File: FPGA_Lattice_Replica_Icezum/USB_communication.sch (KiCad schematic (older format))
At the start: 38 parts, among them J1 USB_Micro_Type_B, U3 FT2232H, U4 DSC1001, U5 93LC56C

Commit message: se finalizo asignación de footprint de acuerdo al modelo original de la icezum alhambra
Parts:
- C18, C19, C20, C21, C23, C25, C26, C27, C28, C29, C30, C33: footprint (none) -> footprints:C_0402
- C32: footprint (none) -> footprints:C_0603
- F1: footprint (none) -> footprints:F_1812
- F2: footprint (none) -> footprints:SOT-563
- J1: footprint (none) -> footprints:USB_Micro-B
- L1: footprint (none) -> footprints:L_0805
- L2, L3: footprint (none) -> footprints:L_0603
- LD8, LD9: footprint (none) -> footprints:LED_0603
- R10, R11, R12, R13, R14, R15, R16, R47, R48: footprint (none) -> footprints:R_0402
- TP8: footprint (none) -> footprints:Via_Test_point
- U3: footprint (none) -> footprints:FTDI-QFN-64
- U4: footprint (none) -> footprints:Xtal-3_2x2_5
- U5: footprint (none) -> footprints:MSOP-8_3x3mm_Pitch0.65mm
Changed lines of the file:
@@
 F 0 "U5" H 8375 5689 60  0000 C CNN
 F 1 "93LC56C" H 8375 5583 60  0000 C CNN
-F 2 "" H 8050 5500 60  0001 C CNN
+F 2 "footprints:MSOP-8_3x3mm_Pitch0.65mm" H 8050 5500 60  0001 C CNN
 F 3 "" H 8050 5500 60  0000 C CNN
 	1    8050 5500
@@
 F 0 "J1" H 9100 800 60  0000 R CNN
 F 1 "USB_Micro_Type_B" H 9400 900 60  0000 R CNN
-F 2 "" H 9450 2000 60  0001 C CNN
+F 2 "footprints:USB_Micro-B" H 9450 2000 60  0001 C CNN
 F 3 "" H 9450 2000 60  0000 C CNN
 	1    9450 2000
@@
 F 0 "F2" V 10631 3057 47  0000 L CNN
 F 1 "ESDUSB" V 10718 3057 47  0000 L CNN
-F 2 "" H 10350 3050 47  0001 C CNN
+F 2 "footprints:SOT-563" H 10350 3050 47  0001 C CNN
 F 3 "" H 10350 3050 47  0000 C CNN
 	1    10300 2950
@@
 F 0 "C33" H 7415 5846 50  0000 L CNN
 F 1 "100 nF" H 7415 5755 50  0000 L CNN
-F 2 "" H 7338 5650 50  0001 C CNN
+F 2 "footprints:C_0402" H 7338 5650 50  0001 C CNN
 F 3 "~" H 7300 5800 50  0001 C CNN
 	1    7300 5800
@@
 F 0 "R12" H 9370 5146 50  0000 L CNN
 F 1 "10K±5% 0.063W" V 9200 4800 50  0000 L CNN
-F 2 "" V 9230 5100 50  0001 C CNN
+F 2 "footprints:R_0402" V 9230 5100 50  0001 C CNN
 F 3 "~" H 9300 5100 50  0001 C CNN
 	1    9300 5100
@@
 F 0 "R13" H 9770 5146 50  0000 L CNN
 F 1 "10K±5% 0.063W" V 9600 4800 50  0000 L CNN
-F 2 "" V 9630 5100 50  0001 C CNN
+F 2 "footprints:R_0402" V 9630 5100 50  0001 C CNN
 F 3 "~" H 9700 5100 50  0001 C CNN
 	1    9700 5100
@@
 F 0 "R14" H 10220 5146 50  0000 L CNN
 F 1 "10K±5% 0.063W" V 10050 4800 50  0000 L CNN
-F 2 "" V 10080 5100 50  0001 C CNN
+F 2 "footprints:R_0402" V 10080 5100 50  0001 C CNN
 F 3 "~" H 10150 5100 50  0001 C CNN
 	1    10150 5100
@@
 F 0 "L2" H 8650 2550 50  0000 R CNN
 F 1 "BLM18SG121TN1D" V 8750 2900 50  0000 R CNN
-F 2 "" H 8650 2550 50  0001 C CNN
+F 2 "footprints:L_0603" H 8650 2550 50  0001 C CNN
 F 3 "~" H 8650 2550 50  0001 C CNN
 	1    8650 2550
@@
 F 0 "F1" H 8275 2294 60  0000 C CNN
 F 1 "0,5 A" H 8275 2188 60  0000 C CNN
-F 2 "" H 7900 2050 60  0001 C CNN
+F 2 "footprints:F_1812" H 7900 2050 60  0001 C CNN
 F 3 "" H 7900 2050 60  0000 C CNN
 	1    7900 2050
@@
 F 0 "C23" V 8798 2900 50  0000 C CNN
 F 1 "100 nF" V 8889 2900 50  0000 C CNN
-F 2 "" H 9088 2750 50  0001 C CNN
+F 2 "footprints:C_0402" H 9088 2750 50  0001 C CNN
 F 3 "~" H 9050 2900 50  0001 C CNN
 	1    9050 2900
@@
 F 0 "C26" H 4215 2396 50  0000 L CNN
 F 1 "100 nF" H 4215 2305 50  0000 L CNN
-F 2 "" H 4138 2200 50  0001 C CNN
+F 2 "footprints:C_0402" H 4138 2200 50  0001 C CNN
 F 3 "~" H 4100 2350 50  0001 C CNN
 	1    4100 2350
@@
 F 0 "C27" H 4815 2396 50  0000 L CNN
 F 1 "100 nF" H 4815 2305 50  0000 L CNN
-F 2 "" H 4738 2200 50  0001 C CNN
+F 2 "footprints:C_0402" H 4738 2200 50  0001 C CNN
 F 3 "~" H 4700 2350 50  0001 C CNN
 	1    4700 2350
@@
 F 0 "C28" H 5415 2396 50  0000 L CNN
 F 1 "100 nF" H 5415 2305 50  0000 L CNN
-F 2 "" H 5338 2200 50  0001 C CNN
+F 2 "footprints:C_0402" H 5338 2200 50  0001 C CNN
 F 3 "~" H 5300 2350 50  0001 C CNN
 	1    5300 2350
@@
 F 0 "C29" H 6065 2396 50  0000 L CNN
 F 1 "100 nF" H 6065 2305 50  0000 L CNN
-F 2 "" H 5988 2200 50  0001 C CNN
+F 2 "footprints:C_0402" H 5988 2200 50  0001 C CNN
 F 3 "~" H 5950 2350 50  0001 C CNN
 	1    5950 2350
@@
 F 0 "C19" H 3665 1596 50  0000 L CNN
 F 1 "100 nF" H 3665 1505 50  0000 L CNN
-F 2 "" H 3588 1400 50  0001 C CNN
+F 2 "footprints:C_0402" H 3588 1400 50  0001 C CNN
 F 3 "~" H 3550 1550 50  0001 C CNN
 	1    3550 1550
@@
 F 0 "C20" H 4215 1596 50  0000 L CNN
 F 1 "100 nF" H 4215 1505 50  0000 L CNN
-F 2 "" H 4138 1400 50  0001 C CNN
+F 2 "footprints:C_0402" H 4138 1400 50  0001 C CNN
 F 3 "~" H 4100 1550 50  0001 C CNN
 	1    4100 1550
@@
 F 0 "C21" H 4765 1596 50  0000 L CNN
 F 1 "100 nF" H 4765 1505 50  0000 L CNN
-F 2 "" H 4688 1400 50  0001 C CNN
+F 2 "footprints:C_0402" H 4688 1400 50  0001 C CNN
 F 3 "~" H 4650 1550 50  0001 C CNN
 	1    4650 1550
@@
 F 0 "C25" H 2815 2396 50  0000 L CNN
 F 1 "100 nF" H 2815 2305 50  0000 L CNN
-F 2 "" H 2738 2200 50  0001 C CNN
+F 2 "footprints:C_0402" H 2738 2200 50  0001 C CNN
 F 3 "~" H 2700 2350 50  0001 C CNN
 	1    2700 2350
@@
 F 0 "C18" H 2815 1596 50  0000 L CNN
 F 1 "100 nF" H 2815 1505 50  0000 L CNN
-F 2 "" H 2738 1400 50  0001 C CNN
+F 2 "footprints:C_0402" H 2738 1400 50  0001 C CNN
 F 3 "~" H 2700 1550 50  0001 C CNN
 	1    2700 1550
@@
 F 0 "L3" V 1700 2200 50  0000 C CNN
 F 1 "BLM18SG121TN1D" V 1600 2200 50  0000 C CNN
-F 2 "" H 1650 2200 50  0001 C CNN
+F 2 "footprints:L_0603" H 1650 2200 50  0001 C CNN
 F 3 "~" H 1650 2200 50  0001 C CNN
 	1    1650 2200
@@
 F 0 "L1" V 1700 1400 50  0000 C CNN
 F 1 "10 uH 0,1 A" V 1600 1400 50  0000 C CNN
-F 2 "" H 1650 1400 50  0001 C CNN
+F 2 "footprints:L_0805" H 1650 1400 50  0001 C CNN
 F 3 "~" H 1650 1400 50  0001 C CNN
 	1    1650 1400
@@
 F 0 "R48" H 5650 6550 50  0000 L CNN
 F 1 "2K2±5% 0.063W" H 5600 6400 50  0000 L CNN
-F 2 "" V 5530 6550 50  0001 C CNN
+F 2 "footprints:R_0402" V 5530 6550 50  0001 C CNN
 F 3 "~" H 5600 6550 50  0001 C CNN
 	1    5600 6550
@@
 F 0 "R47" H 6350 6550 50  0000 L CNN
 F 1 "2K2±5% 0.063W" H 6300 6400 50  0000 L CNN
-F 2 "" V 6230 6550 50  0001 C CNN
+F 2 "footprints:R_0402" V 6230 6550 50  0001 C CNN
 F 3 "~" H 6300 6550 50  0001 C CNN
 	1    6300 6550
@@
 F 0 "LD9" V 5547 7228 50  0000 L CNN
 F 1 "Yellow" V 5638 7228 50  0000 L CNN
-F 2 "" H 5600 7150 50  0001 C CNN
+F 2 "footprints:LED_0603" H 5600 7150 50  0001 C CNN
 F 3 "~" H 5600 7150 50  0001 C CNN
 	1    5600 7150
@@
 F 0 "LD8" V 6247 7228 50  0000 L CNN
 F 1 "Green" V 6338 7228 50  0000 L CNN
-F 2 "" H 6300 7150 50  0001 C CNN
+F 2 "footprints:LED_0603" H 6300 7150 50  0001 C CNN
 F 3 "~" H 6300 7150 50  0001 C CNN
 	1    6300 7150
@@
 F 0 "U4" H 1350 6450 60  0000 C CNN
 F 1 "DSC1001" H 1350 5900 60  0000 C CNN
-F 2 "" H 850 6400 60  0001 C CNN
+F 2 "footprints:Xtal-3_2x2_5" H 850 6400 60  0001 C CNN
 F 3 "" H 850 6400 60  0000 C CNN
 	1    850  6400
@@
 F 0 "C32" H 1465 5746 50  0000 L CNN
 F 1 "10 nF" H 1465 5655 50  0000 L CNN
-F 2 "" H 1388 5550 50  0001 C CNN
+F 2 "footprints:C_0603" H 1388 5550 50  0001 C CNN
 F 3 "~" H 1350 5700 50  0001 C CNN
 	1    1350 5700
@@
 F 0 "R11" H 2030 5054 50  0000 R CNN
 F 1 "12K±1% 0.063W" V 2250 5500 50  0000 R CNN
-F 2 "" V 2030 5100 50  0001 C CNN
+F 2 "footprints:R_0402" V 2030 5100 50  0001 C CNN
 F 3 "~" H 2100 5100 50  0001 C CNN
 	1    2100 5100
@@
 F 0 "R10" H 1320 4596 50  0000 L CNN
 F 1 "2K2±5% 0.063W" H 1320 4505 50  0000 L CNN
-F 2 "" V 1180 4550 50  0001 C CNN
+F 2 "footprints:R_0402" V 1180 4550 50  0001 C CNN
 F 3 "~" H 1250 4550 50  0001 C CNN
 	1    1250 4550
@@
 F 0 "C30" H 1265 3596 50  0000 L CNN
 F 1 "100 nF" H 1265 3505 50  0000 L CNN
-F 2 "" H 1188 3400 50  0001 C CNN
+F 2 "footprints:C_0402" H 1188 3400 50  0001 C CNN
 F 3 "~" H 1150 3550 50  0001 C CNN
 	1    1150 3550
@@
 F 0 "U3" H 2800 7400 60  0000 C CNN
 F 1 "FT2232H" H 2800 7300 60  0000 C CNN
-F 2 "" H 3600 5300 60  0001 C CNN
+F 2 "footprints:FTDI-QFN-64" H 3600 5300 60  0001 C CNN
 F 3 "" H 3600 5300 60  0000 C CNN
 	1    3700 5200
@@
 F 0 "R16" V 1750 7050 50  0000 C CNN
 F 1 "0R±5% 0.063W" V 1950 7050 50  0000 C CNN
-F 2 "" V 1780 7050 50  0001 C CNN
+F 2 "footprints:R_0402" V 1780 7050 50  0001 C CNN
 F 3 "~" H 1850 7050 50  0001 C CNN
 	1    1850 7050
@@
 F 0 "R15" V 10400 6000 50  0000 L CNN
 F 1 "2K2±5% 0.063W" V 10200 5750 50  0000 L CNN
-F 2 "" V 10230 6050 50  0001 C CNN
+F 2 "footprints:R_0402" V 10230 6050 50  0001 C CNN
 F 3 "~" H 10300 6050 50  0001 C CNN
 	1    10300 6050
@@
 F 0 "TP8" H 3628 1242 60  0000 L CNN
 F 1 "TestPoint_Small" H 3550 1050 60  0001 C CNN
-F 2 "" H 3550 1150 60  0001 C CNN
+F 2 "footprints:Via_Test_point" H 3550 1150 60  0001 C CNN
 F 3 "" H 3550 1150 60  0000 C CNN
 	1    3550 1150

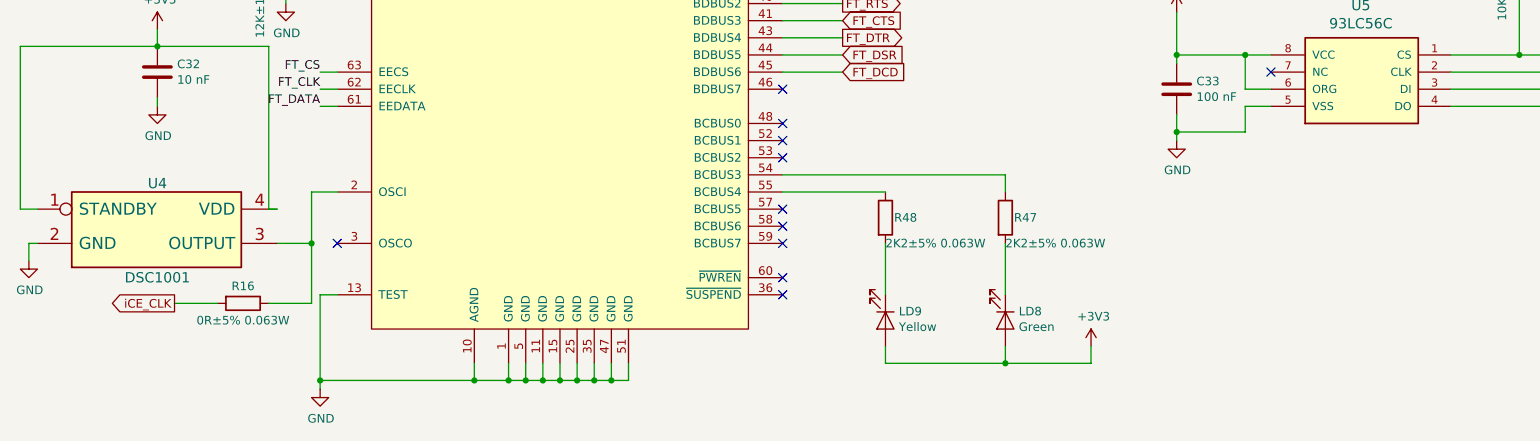
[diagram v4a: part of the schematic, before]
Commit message: se coloco hojas de datos de los componentes
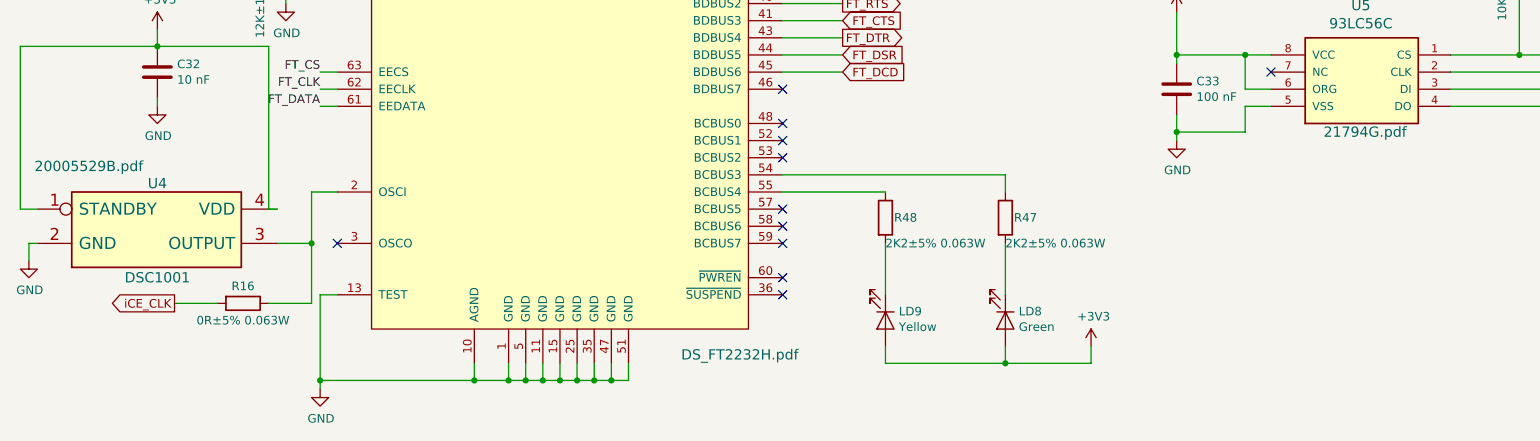
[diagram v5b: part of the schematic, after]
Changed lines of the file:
@@
 F 1 "93LC56C" H 8375 5583 60  0000 C CNN
 F 2 "footprints:MSOP-8_3x3mm_Pitch0.65mm" H 8050 5500 60  0001 C CNN
-F 3 "" H 8050 5500 60  0000 C CNN
+F 3 "21794G.pdf" H 8400 4950 60  0000 C CNN
 	1    8050 5500
 	1    0    0    -1
@@
 F 1 "DSC1001" H 1350 5900 60  0000 C CNN
 F 2 "footprints:Xtal-3_2x2_5" H 850 6400 60  0001 C CNN
-F 3 "" H 850 6400 60  0000 C CNN
+F 3 "20005529B.pdf" H 950 6550 60  0000 C CNN
 	1    850  6400
 	1    0    0    -1
@@
 F 1 "FT2232H" H 2800 7300 60  0000 C CNN
 F 2 "footprints:FTDI-QFN-64" H 3600 5300 60  0001 C CNN
-F 3 "" H 3600 5300 60  0000 C CNN
+F 3 "DS_FT2232H.pdf" H 4750 3050 60  0000 C CNN
 	1    3700 5200
 	1    0    0    -1

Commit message: se corrigieron errores de huellas y referencias que genereban errores cuando se hacia el diseño PCB
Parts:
- LD8, LD9: symbol Device:LED -> icezum:LED
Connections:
- net +3V3: now also LD8.A, LD9.A; no longer LD8.2 (A), LD9.2 (A)
- net at R48.2: now also LD9.K; no longer LD9.1 (K)
- net at R47.2: now also LD8.K; no longer LD8.1 (K)
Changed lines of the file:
@@
 $EndComp
 $Comp
-L Device:LED LD9
+L icezum:LED LD9
 U 1 1 5D2FC05B
-P 5600 7150
-F 0 "LD9" V 5547 7228 50  0000 L CNN
-F 1 "Yellow" V 5638 7228 50  0000 L CNN
-F 2 "footprints:LED_0603" H 5600 7150 50  0001 C CNN
-F 3 "~" H 5600 7150 50  0001 C CNN
-	1    5600 7150
-	0    1    1    0
-$EndComp
-$Comp
-L Device:LED LD8
+P 5600 7350
+F 0 "LD9" V 5650 7450 50  0000 L CNN
+F 1 "Yellow" V 5750 7400 50  0000 L CNN
+F 2 "footprints:LED_0603" H 5600 7350 50  0001 C CNN
+F 3 "~" H 5600 7350 50  0001 C CNN
+	1    5600 7350
+	0    -1   -1   0
+$EndComp
+$Comp
+L icezum:LED LD8
 U 1 1 5D2FC754
-P 6300 7150
-F 0 "LD8" V 6247 7228 50  0000 L CNN
-F 1 "Green" V 6338 7228 50  0000 L CNN
-F 2 "footprints:LED_0603" H 6300 7150 50  0001 C CNN
-F 3 "~" H 6300 7150 50  0001 C CNN
-	1    6300 7150
-	0    1    1    0
+P 6300 7350
+F 0 "LD8" V 6350 7450 50  0000 L CNN
+F 1 "Green" V 6450 7400 50  0000 L CNN
+F 2 "footprints:LED_0603" H 6300 7350 50  0001 C CNN
+F 3 "~" H 6300 7350 50  0001 C CNN
+	1    6300 7350
+	0    -1   -1   0
 $EndComp
 $Comp
@@
 	1700 7050 1450 7050
 Wire Wire Line
-	5600 7300 5600 7400
-Wire Wire Line
-	5600 7400 6300 7400
-Wire Wire Line
 	6800 7400 6800 7300
-Wire Wire Line
-	6300 7300 6300 7400
-Connection ~ 6300 7400
-Wire Wire Line
-	6300 7400 6800 7400
-Wire Wire Line
-	5600 7000 5600 6700
-Wire Wire Line
-	6300 6700 6300 7000
 Wire Wire Line
 	5000 6400 5600 6400
@@
 Wire Wire Line
 	750  2750 750  2600
+Wire Wire Line
+	5600 7400 6300 7400
+Wire Wire Line
+	5600 7350 5600 7400
+Wire Wire Line
+	6300 7350 6300 7400
+Connection ~ 6300 7400
+Wire Wire Line
+	6300 7400 6800 7400
+Wire Wire Line
+	6300 6700 6300 6800
+Wire Wire Line
+	5600 6700 5600 6800
 $EndSCHEMATC
